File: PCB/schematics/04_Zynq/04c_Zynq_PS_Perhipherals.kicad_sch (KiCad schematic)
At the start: 128 parts, among them J1 HR911105A_C12074, J10 I2C_7, J11 3.3V_I2C, J17 I2C_0, J2 USB3_B, J4 I2C_1, J5 I2C_2, J6 I2C_3, J7 I2C_4, J8 I2C_5, J9 I2C_6, U28 MT25QU256ABA8ESF-0SIT TR, U29 FEMDNN032G-A3A55, U30 TXS02612RTWR, U31 DP83867IRRGZR, U32 USB3320C-EZK-TR, U33 TPD4E05U06DQA, U34 CP2102N-A02-GQFN24, U35 TXB0108PW, U36 TCA9548APWR, U37 PCA9306, Y1 25 MHz, Y2 25 MHz

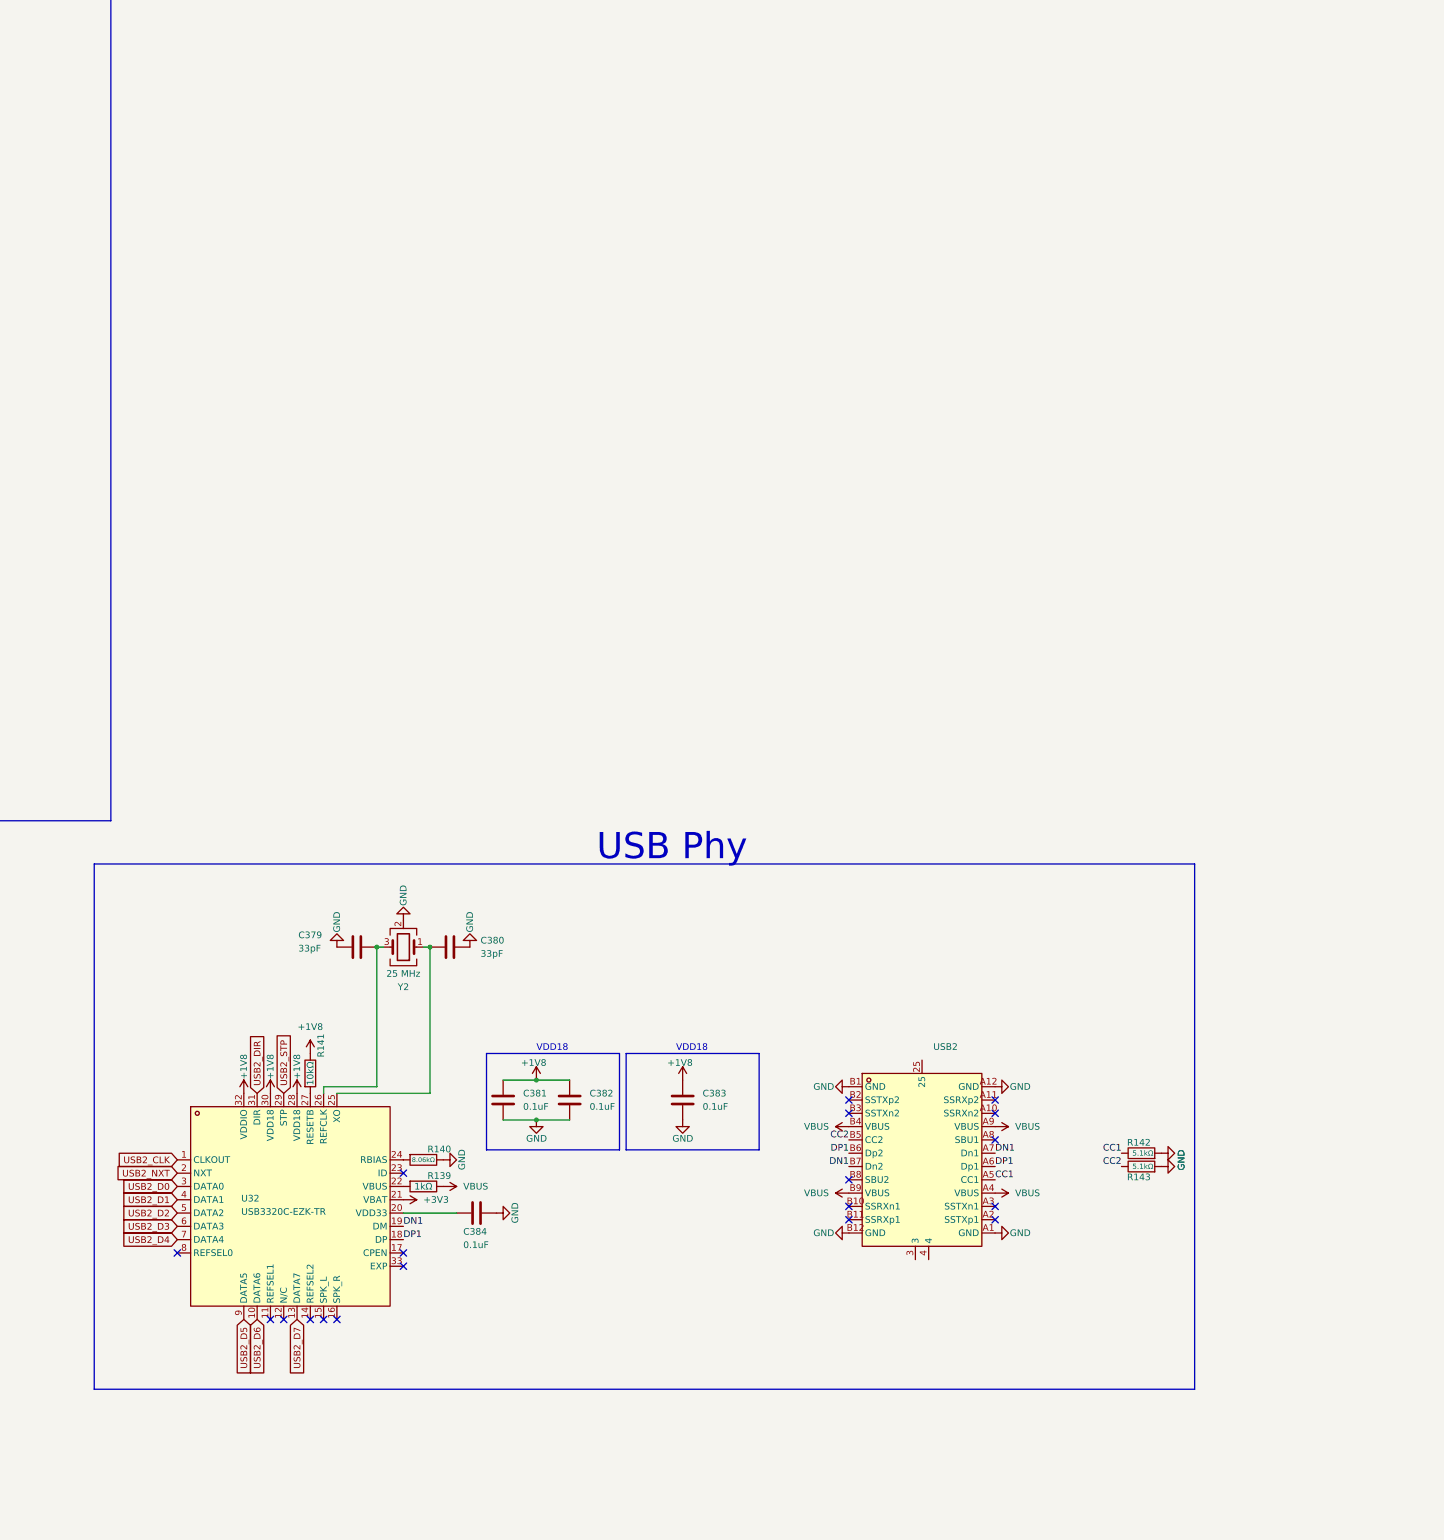
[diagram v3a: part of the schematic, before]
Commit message: High Speed Peripherals added
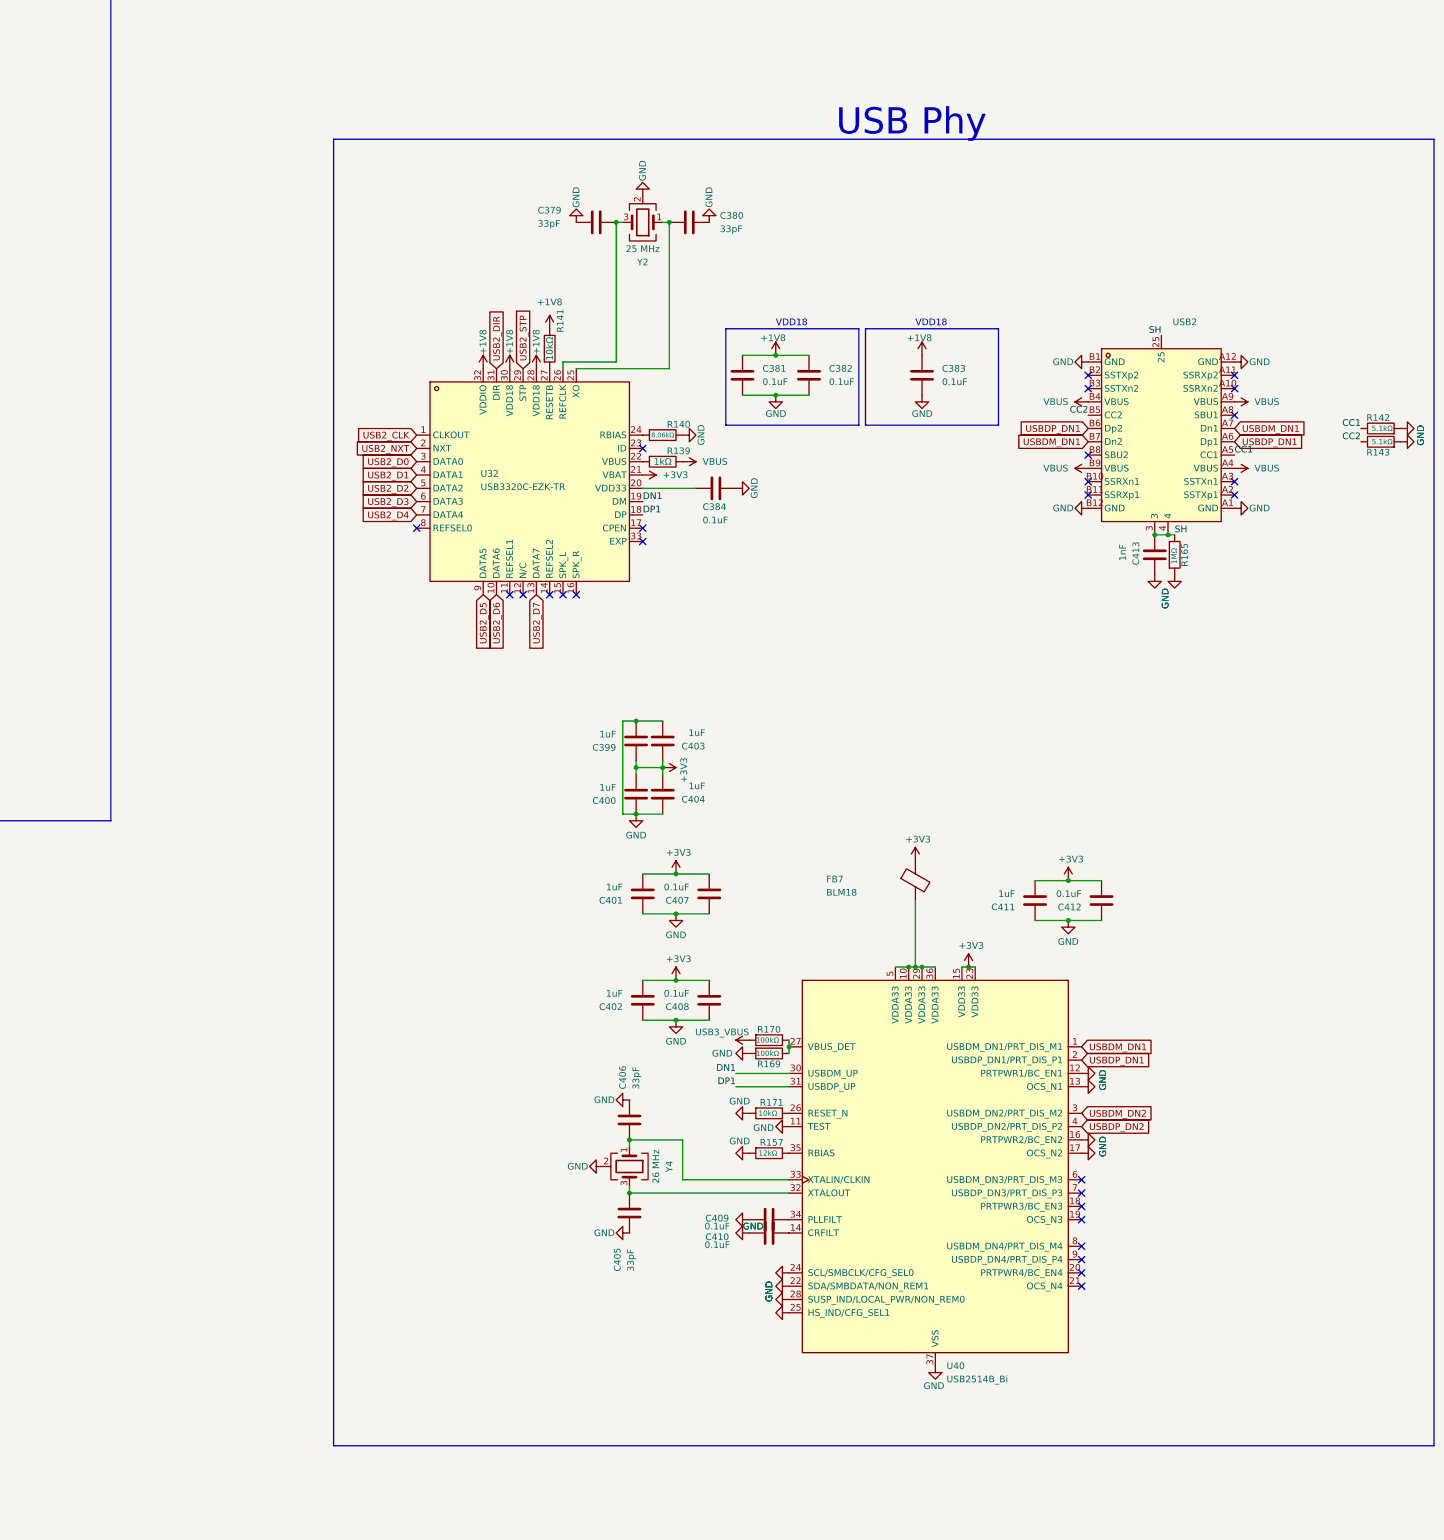
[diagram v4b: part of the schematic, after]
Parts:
- added C399, C400, C401, C402, C403, C404, C411: 1uF, Capacitor_SMD:C_0402_1005Metric, symbol Device:C
- added C405, C406: 33pF, Capacitor_SMD:C_0402_1005Metric, symbol Device:C
- added C407, C408, C409, C410, C412: 0.1uF, Capacitor_SMD:C_0402_1005Metric, symbol Device:C
- added C413: 1nF, Capacitor_SMD:C_0402_1005Metric, symbol Device:C
- added FB7: BLM18, Inductor_SMD:L_01005_0402Metric, symbol Device:FerriteBead
- added R157: 12kΩ, Resistor_SMD:R_0402_1005Metric, symbol Device:R
- added R165: 1MΩ, Resistor_SMD:R_0402_1005Metric, symbol Device:R
- added R169, R170: 100kΩ, Resistor_SMD:R_0402_1005Metric, symbol Device:R
- added R171: 10kΩ, Resistor_SMD:R_0402_1005Metric, symbol Device:R
- added U40: USB2514B_Bi, Package_DFN_QFN:QFN-36-1EP_6x6mm_P0.5mm_EP3.7x3.7mm, symbol Interface_USB:USB2514B_Bi
- added Y4: 26 MHz, Crystal:Crystal_SMD_3225-4Pin_3.2x2.5mm, symbol Device:Crystal_GND24
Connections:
- net +3V3: now also C399.1, C400.2, C401.2, C402.2, C403.1, C404.2, C407.2, C408.2, C411.2, C412.2, FB7.1, U40.15 (VDD33), U40.23 (VDD33)
- net DN1: now also U40.30 (USBDM_UP); no longer USB2.A7 (Dn1), USB2.B7 (Dn2)
- net DP1: now also U40.31 (USBDP_UP); no longer USB2.A6 (Dp1), USB2.B6 (Dp2)
- net GND: now also C399.2, C400.1, C401.1, C402.1, C403.2, C404.1, C405.1, C406.1, C407.1, C408.1, C409.2, C410.2, C411.1, C412.1, C413.1, R157.2, R165.2, R169.2, R171.2, U40.11 (TEST), U40.12 (PRTPWR1/BC_EN1), U40.13 (OCS_N1), U40.16 (PRTPWR2/BC_EN2), U40.17 (OCS_N2), U40.22 (SDA/SMBDATA/NON_REM1), U40.24 (SCL/SMBCLK/CFG_SEL0), U40.25 (HS_IND/CFG_SEL1), U40.28 (SUSP_IND/LOCAL_PWR/NON_REM0), U40.37 (VSS), Y4.2 (G), Y4.4 (G)
- net SH: now reaches USB2.25
- net SH: now also USB2.3, USB2.4, C413.2, R165.1
- new net: R169.1, R170.1, U40.27 (VBUS_DET)
- new net: C406.2, U40.33 (XTALIN/CLKIN), Y4.1
- new net: C405.2, U40.32 (XTALOUT), Y4.3
- new net: R171.1, U40.26 (RESET_N)
- new net: C409.1, U40.34 (PLLFILT)
- new net: C410.1, U40.14 (CRFILT)
- new net: FB7.2, U40.10 (VDDA33), U40.29 (VDDA33), U40.36 (VDDA33), U40.5 (VDDA33)
- new net: R157.1, U40.35 (RBIAS)
- new net USB3_VBUS: R170.2
- new net USBDM_DN1: U40.1 (USBDM_DN1/PRT_DIS_M1), USB2.A7 (Dn1), USB2.B7 (Dn2)
- new net USBDM_DN2: U40.3 (USBDM_DN2/PRT_DIS_M2)
- new net USBDP_DN1: U40.2 (USBDP_DN1/PRT_DIS_P1), USB2.A6 (Dp1), USB2.B6 (Dp2)
- new net USBDP_DN2: U40.4 (USBDP_DN2/PRT_DIS_P2)
- no-connect marks 198 -> 206
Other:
- moved on the sheet: C379, C380, C381, C382, C383, C384, R139, R140, R141, R142, R143, U32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

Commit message: Feat : Schematics Complete
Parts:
- removed J10: I2C_7, Connector_PinHeader_2.54mm:PinHeader_1x02_P2.54mm_Vertical, symbol Connector:Conn_01x02_Pin
- removed J17: I2C_0, Connector_PinHeader_2.54mm:PinHeader_1x02_P2.54mm_Vertical, symbol Connector:Conn_01x02_Pin
- removed J4: I2C_1, Connector_PinHeader_2.54mm:PinHeader_1x02_P2.54mm_Vertical, symbol Connector:Conn_01x02_Pin
- removed J5: I2C_2, Connector_PinHeader_2.54mm:PinHeader_1x02_P2.54mm_Vertical, symbol Connector:Conn_01x02_Pin
- removed J6: I2C_3, Connector_PinHeader_2.54mm:PinHeader_1x02_P2.54mm_Vertical, symbol Connector:Conn_01x02_Pin
- removed J7: I2C_4, Connector_PinHeader_2.54mm:PinHeader_1x02_P2.54mm_Vertical, symbol Connector:Conn_01x02_Pin
- removed J8: I2C_5, Connector_PinHeader_2.54mm:PinHeader_1x02_P2.54mm_Vertical, symbol Connector:Conn_01x02_Pin
- removed J9: I2C_6, Connector_PinHeader_2.54mm:PinHeader_1x02_P2.54mm_Vertical, symbol Connector:Conn_01x02_Pin
- added C504: 0.1uF, Capacitor_SMD:C_0402_1005Metric, symbol Device:C
- added J10: Conn_02x07_Odd_Even, Connector_PinHeader_2.54mm:PinHeader_2x07_P2.54mm_Vertical, symbol Connector_Generic:Conn_02x07_Odd_Even
- added J11: Conn_01x04_Pin, Connector_PinHeader_2.54mm:PinHeader_1x04_P2.54mm_Vertical, symbol Connector:Conn_01x04_Pin
- added R162, R198: 10kΩ, Resistor_SMD:R_0402_1005Metric, symbol Device:R
- added R199, R200: 2.2kΩ, Resistor_SMD:R_0402_1005Metric, symbol Device:R
- added U53: TCA9548APWR, Package_SO:TSSOP-24_4.4x7.8mm_P0.65mm, symbol Interface_Expansion:TCA9548APWR
- U33: renamed from U32; footprint Connector_USB:USB3_A_Plug_Wuerth_692112030100_Horizontal -> Devboard_Footprints:RJ45-TH_HR911105A
- renumbered C346 to C341, C348 to C342, C350 to C343, C352 to C344, C338 to C345, C339 to C346, C340 to C347, C341 to C348, C347 to C349, C349 to C350, C353 to C352, C360 to C353, C342 to C354, C343 to C355, C344 to C356, C345 to C357, C354 to C358, C355 to C359, C337 to C360, C356 to C361, C357 to C362, C358 to C363, C359 to C364, C361 to C365, C362 to C366, C363 to C367, C364 to C368, C365 to C369, C366 to C370, C378 to C371, C379 to C372, C380 to C373, C377 to C374, C367 to C376, C369 to C377, C371 to C378, C373 to C379, C368 to C380, C370 to C381, C372 to C382, C374 to C383, C386 to C384, C376 to C385, C381 to C386, C382 to C387, C383 to C388, C385 to C389, C384 to C390, C387 to C391, C413 to C392, C399 to C393, C403 to C394, C400 to C395, C404 to C396, C388 to C397, C401 to C398, C407 to C399, C411 to C400, C412 to C401, C392 to C402, C391 to C403, C402 to C404, C408 to C405, C390 to C406, C389 to C407, C406 to C408, C405 to C409, C409 to C410, C410 to C411, FB7 to FB9, J2 to J3, J11 to J6, R117 to R110, R2 to R112, R112 to R114, R110 to R115, R114 to R116, R118 to R117, R119 to R118, R120 to R119, R121 to R120, R122 to R121, R116 to R122, R115 to R123, R136 to R124, R127 to R125, R128 to R126, R129 to R127, R130 to R128, R137 to R129, R141 to R130, R138 to R132, R123 to R133, R124 to R134, R142 to R135, R125 to R136, R140 to R137, R143 to R138, R126 to R139, R139 to R140, R132 to R141, R133 to R142, R134 to R143, R135 to R144, R146 to R145, R144 to R146, R145 to R147, R165 to R148, R147 to R149, R148 to R150, R149 to R151, R155 to R152, R170 to R153, R169 to R155, R152 to R156, R150 to R157, R171 to R158, R153 to R159, R151 to R160, R157 to R161, U30 to U28, U28 to U29, U29 to U30, U34 to U32, U33 to U34, U36 to U35, U35 to U36, U40 to U38, Y2 to Y1, Y1 to Y2, Y4 to Y3
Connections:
- net +1V8: now also C504.1, R198.1, R199.1, R200.1, U53.1 (A0), U53.2 (A1), U53.21 (A2), U53.24 (VCC)
- net +3V3: now also J10.2 (Pin_2), R162.1
- net +5V_SYS: now also J11.2 (Pin_2)
- net GND: now also J3.4 (GND), J3.SH (SHIELD), C504.2, J10.1 (Pin_1), J10.11 (Pin_11), J10.13 (Pin_13), J10.3 (Pin_3), J10.5 (Pin_5), J10.7 (Pin_7), J10.9 (Pin_9), J11.1 (Pin_1), U53.12 (GND)
- net I2C1_SCL: now also U53.22 (SCL)
- net I2C1_SDA: now also U53.23 (SDA)
- net I2C_SCL_2: now also U36.3 (A2)
- net I2C_SDA_2: now also U36.1 (A1)
- net VBUS: no longer J3.1 (VBUS), R147.1
- net E_XI: now reaches C385.2, U31.15 (X_I), Y2.1
- net I2C_SCL_2_T: now reaches U36.18 (B2)
- net I2C_SDA_2_T: now reaches U36.20 (B1)
- net USB_REFCLK: now reaches C372.2, U33.26 (REFCLK), Y1.3
- new net: J11.4 (Pin_4), R162.2
- new net: R198.2, U53.3 (~{RESET})
- new net: J3.1 (VBUS), R147.1
- new net FAN_TACH: J11.3 (Pin_3)
- new net I2C_SCL1_0: R199.2, U53.5 (SC0)
- new net I2C_SCL1_1: U53.7 (SC1)
- new net I2C_SCL1_2: U53.9 (SC2)
- new net I2C_SCL1_3: U53.11 (SC3)
- new net I2C_SCL1_4: U53.14 (SC4)
- new net I2C_SCL1_5: U53.16 (SC5)
- new net I2C_SCL1_6: U53.18 (SC6)
- new net I2C_SCL1_7: U53.20 (SC7)
- new net I2C_SDA1_0: R200.2, U53.4 (SD0)
- new net I2C_SDA1_1: U53.6 (SD1)
- new net I2C_SDA1_2: U53.8 (SD2)
- new net I2C_SDA1_3: U53.10 (SD3)
- new net I2C_SDA1_4: U53.13 (SD4)
- new net I2C_SDA1_5: U53.15 (SD5)
- new net I2C_SDA1_6: U53.17 (SD6)
- new net I2C_SDA1_7: U53.19 (SD7)
- new net PS_JTAG_TCK: J10.6 (Pin_6)
- new net PS_JTAG_TDI: J10.10 (Pin_10)
- new net PS_JTAG_TDO: J10.8 (Pin_8)
- new net PS_JTAG_TMS: J10.4 (Pin_4)
- new net PS_SRST_B: J10.12 (Pin_12)
- no-connect marks 206 -> 213
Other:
- note added: "JTAG Header + Fan"
- note added: "Section 04c : Peripherals"
- moved on the sheet: C341, C342, C343, C344, C345, C346, C347, C348, C349, C350, C351, C352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

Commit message: Refactor : Repo
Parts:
- U33: footprint Devboard_Footprints:RJ45-TH_HR911105A -> Devboard_Footprints:QFN-32_L5.0-W5.0-P0.50-BL-EP3.4
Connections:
- net GND: no longer J3.SH (SHIELD)
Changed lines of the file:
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@@
 	)
 	(rectangle
-		(start 12.065 12.065)
-		(end 828.675 81.915)
+		(start 12.065 72.39)
+		(end 41.91 81.915)
 		(stroke
 			(width 0)
@@
 	)
 	(rectangle
+		(start 12.065 12.065)
+		(end 828.675 81.915)
+		(stroke
+			(width 0)
+			(type solid)
+		)
+		(fill
+			(type color)
+			(color 255 229 191 1)
+		)
+	)
+	(rectangle
 		(start 337.185 173.355)
 		(end 495.935 236.22)
@@
 		(pin "7"
 		)
-		(pin "SH"
-		)
 		(pin "5"
 		)
@@
 	)
 	(symbol
-		(lib_id "power:GND")
-		(at 502.92 535.94 90)
-		(unit 1)
-		(body_style 1)
-		(exclude_from_sim no)
-		(in_bom yes)
-		(on_board yes)
-		(in_pos_files yes)
-		(dnp no)
-		(property "Reference" "#PWR01086"
-			(at 509.27 535.94 0)
-			(hide yes)
-			(show_name no)
-			(do_not_autoplace no)
-			(effects
-				(font
-					(size 1.27 1.27)
-				)
-			)
-		)
-		(property "Value" "GND"
-			(at 506.476 533.908 0)
-			(show_name no)
-			(do_not_autoplace no)
-			(effects
-				(font
-					(size 1.27 1.27)
-				)
-				(justify right)
-			)
-		)
-		(property "Footprint" ""
-			(at 502.92 535.94 0)
-			(hide yes)
-			(show_name no)
-			(do_not_autoplace no)
-			(effects
-				(font
-					(size 1.27 1.27)
-				)
-			)
-		)
-		(property "Datasheet" ""
-			(at 502.92 535.94 0)
-			(hide yes)
-			(show_name no)
-			(do_not_autoplace no)
-			(effects
-				(font
-					(size 1.27 1.27)
-				)
-			)
-		)
-		(property "Description" "Power symbol creates a global label with name \"GND\" , ground"
-			(at 502.92 535.94 0)
-			(hide yes)
-			(show_name no)
-			(do_not_autoplace no)
-			(effects
-				(font
-					(size 1.27 1.27)
-				)
-			)
-		)
-		(pin "1"
-		)
-		(instances
-			(project "Devboard"
-				(path "/f4f7837f-dd80-4f77-b150-4534de1c10d6/b48c92d5-ffe6-40f3-9dff-a09c41a730f7/3c4a5d01-ee05-4aff-9ef4-dbc6214ba286"
-					(reference "#PWR01086")
-					(unit 1)
-				)
-			)
-		)
-	)
-	(symbol
 		(lib_id "Devboard_Custom:FEMDNN032G-A3A55")
 		(at 666.75 247.65 270)
@@
 	(symbol
 		(lib_id "power:PWR_FLAG")
-		(at 27.94 35.56 270)
+		(at 27.94 76.2 270)
 		(unit 1)
 		(body_style 1)
@@
 		(fields_autoplaced yes)
 		(property "Reference" "#FLG01"
-			(at 29.845 35.56 0)
+			(at 29.845 76.2 0)
 			(hide yes)
 			(show_name no)
@@
 		)
 		(property "Value" "PWR_FLAG"
-			(at 31.75 35.5599 90)
+			(at 31.75 76.1999 90)
 			(show_name no)
 			(do_not_autoplace no)
@@
 		)
 		(property "Footprint" ""
-			(at 27.94 35.56 0)
+			(at 27.94 76.2 0)
 			(hide yes)
 			(show_name no)
@@
 		)
 		(property "Datasheet" ""
-			(at 27.94 35.56 0)
+			(at 27.94 76.2 0)
 			(hide yes)
 			(show_name no)
@@
 		)
 		(property "Description" "Special symbol for telling ERC where power comes from"
-			(at 27.94 35.56 0)
+			(at 27.94 76.2 0)
 			(hide yes)
 			(show_name no)
@@
 			)
 		)
-		(property "Footprint" "Devboard_Footprints:RJ45-TH_HR911105A"
+		(property "Footprint" "Devboard_Footprints:QFN-32_L5.0-W5.0-P0.50-BL-EP3.4"
 			(at 641.35 455.93 0)
 			(hide yes)
@@
 	(symbol
 		(lib_id "power:+3V3")
-		(at 27.94 35.56 90)
+		(at 27.94 76.2 90)
 		(unit 1)
 		(body_style 1)
@@
 		(dnp no)
 		(property "Reference" "#PWR01087"
-			(at 31.75 35.56 0)
+			(at 31.75 76.2 0)
 			(hide yes)
 			(show_name no)
@@
 		)
 		(property "Value" "USB3_VBUS"
-			(at 27.94 34.036 90)
+			(at 24.638 76.2 90)
 			(show_name no)
 			(do_not_autoplace no)
@@
 		)
 		(property "Footprint" ""
-			(at 27.94 35.56 0)
+			(at 27.94 76.2 0)
 			(hide yes)
 			(show_name no)
@@
 		)
 		(property "Datasheet" ""
-			(at 27.94 35.56 0)
+			(at 27.94 76.2 0)
 			(hide yes)
 			(show_name no)
@@
 		)
 		(property "Description" "Power symbol creates a global label with name \"+3V3\""
-			(at 27.94 35.56 0)
+			(at 27.94 76.2 0)
 			(hide yes)
 			(show_name no)

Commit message: Feat : Finished four sections of Placement
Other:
- moved on the sheet: C397, R149, R150, R151, U35
